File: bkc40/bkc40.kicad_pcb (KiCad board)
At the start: 2 copper layers, 266.7 x 76.2 mm, 107 parts, among them J1 Conn_01x02, SW1 SW_Push, SW10 SW_Push, SW11 SW_Push, SW12 SW_Push, SW13 SW_Push, SW14 SW_Push, SW15 SW_Push, SW16 SW_Push, SW17 SW_Push, SW18 SW_Push, SW19 SW_Push, SW2 SW_Push, SW20 SW_Push, SW21 SW_Push, SW22 SW_Push, SW23 SW_Push, SW24 SW_Push, SW25 SW_Push, SW26 SW_Push, SW27 SW_Push, SW28 SW_Push, SW29 SW_Push, SW3 SW_Push, SW30 SW_Push, SW31 SW_Push, SW32 SW_Push, SW33 SW_Push, SW34 SW_Push, SW35 SW_Push, SW36 SW_Push, SW37 SW_Push, SW38 SW_Push, SW39 SW_Push, SW4 SW_Push, SW40 SW_Push, SW41 SW_Push, SW42 SW_Push, SW43 SW_Push, SW44 SW_Push, SW45 SW_Push, SW46 SW_Push, SW47 SW_Push, SW48 SW_Push, SW49 SW_Push, SW5 SW_Push, SW50 SW_Push, SW51 SW_Push, SW52 SW_Push, SW53 SW_Push, SW54 SW_Push, SW55 SW_Push, SW56 Rotary_Encoder_Switch, SW57 SW_Push, SW6 SW_Push, SW7 SW_Push, SW8 SW_Push, SW9 SW_Push, U1 ATmega32U4-AU, Y1 Crystal_GND24_Small

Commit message: v02
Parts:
- removed the G*** at (134.0, 115.1)
- removed U1: ATmega32U4-AU, Package_QFP:TQFP-44_10x10mm_P0.8mm
- added G***: LOGO, silk:turtle_pan_800_bmask, B.Cu at (287.8, 145.4)
- added U2: ATmega32U4-MU, Package_DFN_QFN:QFN-44-1EP_7x7mm_P0.5mm_EP5.2x5.2mm, B.Cu at (143.4, 110.8)
- moved J1 243.5 mm to (118.2, 102.9), turned to 0 degrees
- moved C7 212.0 mm to (151.3, 100.2)
- moved C8 212.0 mm to (145.0, 100.3)
- moved Y1 212.0 mm to (148.2, 100.2)
- moved C1 211.9 mm to (149.3, 112.0)
- moved C2 211.5 mm to (137.2, 111.7)
- moved R4 210.2 mm to (144.2, 116.9), turned to 45 degrees
- moved C5 209.8 mm to (145.1, 104.9)
- moved C9 206.0 mm to (141.5, 103.3), turned to 45 degrees
- moved R1 205.3 mm to (146.1, 103.9), turned to 135 degrees
- moved C6 204.6 mm to (142.6, 104.2), turned to 45 degrees
- moved C4 204.0 mm to (138.4, 107.3)
- moved C3 201.8 mm to (140.9, 116.7), turned to 180 degrees
- moved D21 18.0 mm to (354.7, 120.3)
- moved C10 13.3 mm to (146.6, 80.8)
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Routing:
- net ENC_B: track 69.3 -> 355.2 mm, vias 1 -> 0
- net ENC_A: track 61.0 -> 346.5 mm, vias 1 -> 0
- net +5V: track 308.8 -> 67.9 mm, vias 4 -> 6
- net COL00: track 328.0 -> 91.4 mm, vias 0 -> 1
- net COL01: track 296.4 -> 72.4 mm
- net COL12: track 80.6 -> 297.0 mm
- net D-: track 226.1 -> 13.4 mm
- net D+: track 225.2 -> 13.7 mm
- net COL11: track 102.2 -> 287.9 mm, vias 0 -> 1
- net COL02: track 275.5 -> 93.5 mm
- net COL10: track 105.6 -> 249.1 mm, vias 0 -> 1
- net COL03: track 252.5 -> 115.2 mm
- net COL04: track 232.9 -> 112.1 mm
- net COL09: track 124.9 -> 228.8 mm, vias 0 -> 1
- net COL08: track 123.4 -> 187.7 mm, vias 0 -> 1
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
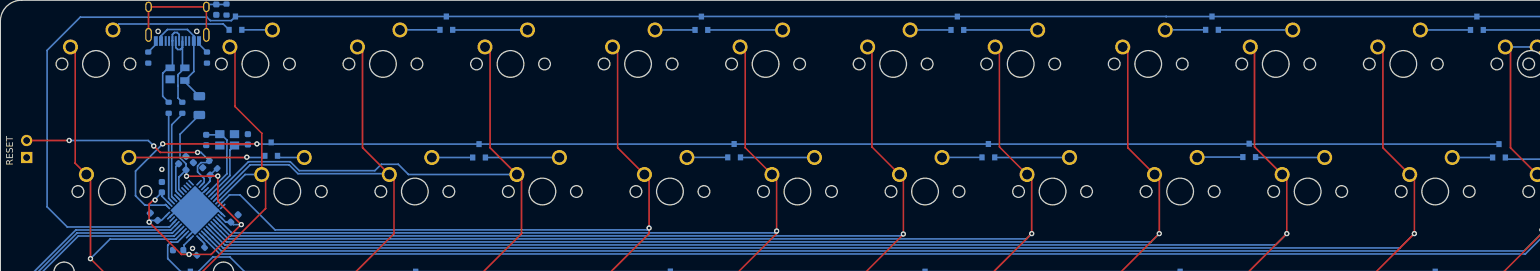
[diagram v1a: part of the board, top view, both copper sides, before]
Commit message: update cc pins
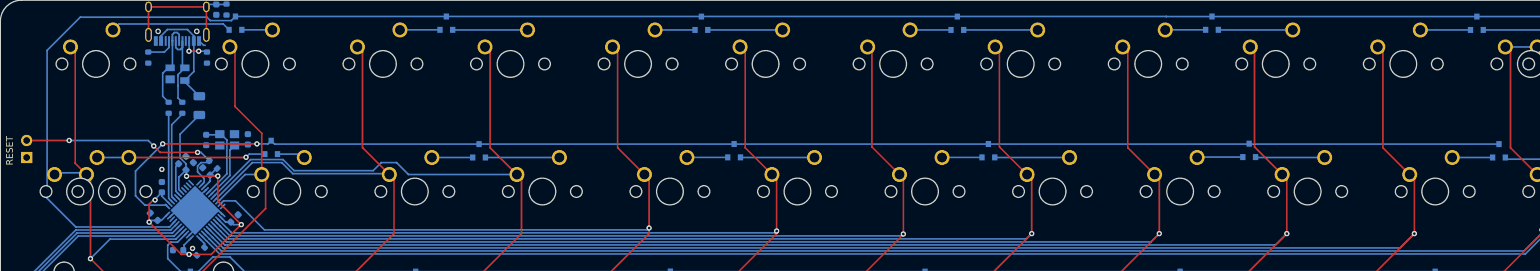
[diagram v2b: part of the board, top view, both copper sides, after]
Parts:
- added SW58: SW_Push, MX_Only:MXOnly-1.25U-NoLED, F.Cu at (126.2, 108.0)
- moved D8 0.25 mm to (154.8, 101.4)
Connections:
- USB1 pad 1: Net-(R5-Pad2) -> GND
- USB1 pad 10: Net-(USB1-Pad10) -> Net-(R6-Pad2)
- USB1 pad 12: Net-(R6-Pad2) -> GND
- USB1 pad 4: Net-(USB1-Pad4) -> Net-(R5-Pad2)
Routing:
- net COL00: track 91.4 -> 96.4 mm
- net Net-(D8-Pad2): track 20.3 -> 25.3 mm
- net Net-(R5-Pad2): track 2.12 -> 4.35 mm
- net GND: track 20.1 -> 22.2 mm
- net Net-(R6-Pad2): track 2.14 -> 4.27 mm, vias 0 -> 2
- net ROW00: track 283.2 -> 282.4 mm
- net COL04: track 112.1 -> 111.4 mm

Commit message: PCB update
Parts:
- moved J1 7.39 mm to (117.6, 110.2)
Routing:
- net Net-(J1-Pad2): track 34.2 -> 39.1 mm
- net ROW00: track 282.4 -> 284.7 mm
- net COL12: track 297.0 -> 297.5 mm
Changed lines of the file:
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@@
     (thickness 1.6)
     (drawings 11)
-    (tracks 572)
+    (tracks 573)
     (zones 0)
     (modules 108)
@@
   )
   (module Connector_PinHeader_2.54mm:PinHeader_1x02_P2.54mm_Vertical (layer B.Cu)
-    (at 118.237 102.87)
+    (at 117.602 110.236)
     (descr "Through hole straight pin header, 1x02, 2.54mm pitch, single row")
     (tags "Through hole pin header THT 1x02 2.54mm single row")
@@
     (effects (font (size 1 1) (thickness 0.15)) (justify mirror))
   )
-  (gr_text RESET (at 115.697 101.853999 90) (layer F.SilkS)
+  (gr_text RESET (at 115.316 109.092999 90) (layer F.SilkS)
     (effects (font (size 1 1) (thickness 0.15)))
   )
-  (gr_text RESET (at 115.697 101.853999 90) (layer B.SilkS)
+  (gr_text RESET (at 115.316 109.092999 90) (layer B.SilkS)
     (effects (font (size 1 1) (thickness 0.15)) (justify mirror))
   )
@@
   (segment (start 356.967 81.82) (end 357.632 81.155) (width 0.25) (layer B.Cu) (net 1))
   (segment (start 334.838 81.82) (end 356.967 81.82) (width 0.25) (layer B.Cu) (net 1))
-  (segment (start 140.315924 112.497796) (end 140.315924 112.427101) (width 0.25) (layer B.Cu) (net 1))
-  (segment (start 121.285 86.868) (end 121.285 108.966) (width 0.25) (layer B.Cu) (net 1))
-  (segment (start 126.238 81.915) (end 121.285 86.868) (width 0.25) (layer B.Cu) (net 1))
+  (segment (start 119.634 88.519) (end 119.634 108.839) (width 0.25) (layer B.Cu) (net 1))
+  (segment (start 124.042001 113.247001) (end 139.566719 113.247001) (width 0.25) (layer B.Cu) (net 1))
+  (segment (start 126.238 81.915) (end 119.634 88.519) (width 0.25) (layer B.Cu) (net 1))
+  (segment (start 119.634 108.839) (end 124.042001 113.247001) (width 0.25) (layer B.Cu) (net 1))
   (segment (start 145.161 81.915) (end 126.238 81.915) (width 0.25) (layer B.Cu) (net 1))
-  (segment (start 125.566001 113.247001) (end 139.566719 113.247001) (width 0.25) (layer B.Cu) (net 1))
-  (segment (start 121.285 108.966) (end 125.566001 113.247001) (width 0.25) (layer B.Cu) (net 1))
+  (segment (start 145.669 82.423) (end 145.161 81.915) (width 0.25) (layer B.Cu) (net 1))
   (segment (start 148.799 82.423) (end 145.669 82.423) (width 0.25) (layer B.Cu) (net 1))
+  (segment (start 140.315924 112.497796) (end 140.315924 112.427101) (width 0.25) (layer B.Cu) (net 1))
   (segment (start 139.566719 113.247001) (end 140.315924 112.497796) (width 0.25) (layer B.Cu) (net 1))
-  (segment (start 145.669 82.423) (end 145.161 81.915) (width 0.25) (layer B.Cu) (net 1))
   (segment (start 149.418 81.804) (end 148.799 82.423) (width 0.25) (layer B.Cu) (net 1))
   (segment (start 147.595 82.931) (end 148.468 83.804) (width 0.25) (layer B.Cu) (net 2))
@@
   (segment (start 365.29875 95.9) (end 365.28375 95.885) (width 0.25) (layer B.Cu) (net 54))
   (segment (start 368.987 95.9) (end 365.29875 95.9) (width 0.25) (layer B.Cu) (net 54))
-  (via (at 366.268 113.665) (size 0.8) (drill 0.4) (layers F.Cu B.Cu) (net 54))
-  (segment (start 366.268 113.792) (end 366.268 113.665) (width 0.25) (layer F.Cu) (net 54))
   (segment (start 366.268 96.647) (end 366.268 113.792) (width 0.25) (layer F.Cu) (net 54))
   (segment (start 366.268 113.792) (end 366.268 118.71325) (width 0.25) (layer F.Cu) (net 54))
-  (segment (start 145.096334 115.316) (end 144.328755 114.548421) (width 0.25) (layer B.Cu) (net 54))
-  (segment (start 147.059324 117.27899) (end 145.096334 115.316) (width 0.25) (layer B.Cu) (net 54))
-  (segment (start 342.08001 117.27899) (end 147.059324 117.27899) (width 0.25) (layer B.Cu) (net 54))
-  (segment (start 345.694 113.665) (end 342.08001 117.27899) (width 0.25) (layer B.Cu) (net 54))
-  (segment (start 366.268 113.665) (end 345.694 113.665) (width 0.25) (layer B.Cu) (net 54))
+  (via (at 366.268 113.283996) (size 0.8) (drill 0.4) (layers F.Cu B.Cu) (net 54))
+  (segment (start 147.059324 117.27899) (end 342.08001 117.27899) (width 0.25) (layer B.Cu) (net 54))
+  (segment (start 366.268 113.792) (end 366.268 113.283996) (width 0.25) (layer F.Cu) (net 54))
+  (segment (start 144.328755 114.548421) (end 147.059324 117.27899) (width 0.25) (layer B.Cu) (net 54))
+  (segment (start 342.08001 117.27899) (end 346.075004 113.283996) (width 0.25) (layer B.Cu) (net 54))
+  (segment (start 346.075004 113.283996) (end 366.268 113.283996) (width 0.25) (layer B.Cu) (net 54))
   (segment (start 131.41325 123.952) (end 131.92125 124.46) (width 0.25) (layer B.Cu) (net 55))
   (segment (start 122.90425 123.952) (end 131.41325 123.952) (width 0.25) (layer B.Cu) (net 55))
@@
   (segment (start 143.383 113.602666) (end 143.383 110.774239) (width 0.25) (layer B.Cu) (net 66))
   (segment (start 142.437245 114.548421) (end 143.383 113.602666) (width 0.25) (layer B.Cu) (net 66))
+  (segment (start 137.528 85.471) (end 137.528 85.992) (width 0.25) (layer B.Cu) (net 66))
+  (segment (start 143.978 85.471) (end 143.978 85.939) (width 0.25) (layer B.Cu) (net 66))
+  (segment (start 143.978 85.471) (end 144.018 85.471) (width 0.25) (layer B.Cu) (net 66))
+  (segment (start 144.018 85.471) (end 144.653 86.106) (width 0.25) (layer B.Cu) (net 66))
+  (segment (start 144.653 86.106) (end 144.907 86.106) (width 0.25) (layer B.Cu) (net 66))
   (segment (start 138.353705 112.268) (end 139.255264 111.366441) (width 0.25) (layer B.Cu) (net 67))
   (segment (start 147.959188 112.522) (end 147.157182 111.719994) (width 0.25) (layer B.Cu) (net 67))
@@
   (segment (start 145.796 103.632) (end 144.272 103.632) (width 0.25) (layer B.Cu) (net 74))
   (via (at 124.587 100.33) (size 0.8) (drill 0.4) (layers F.Cu B.Cu) (net 74))
-  (segment (start 118.237 100.33) (end 124.587 100.33) (width 0.25) (layer F.Cu) (net 74))
   (via (at 137.218847 101.150847) (size 0.8) (drill 0.4) (layers F.Cu B.Cu) (net 74))
   (segment (start 136.398 100.33) (end 137.218847 101.150847) (width 0.25) (layer B.Cu) (net 74))
@@
   (segment (start 144.272 102.108) (end 145.518274 103.354274) (width 0.25) (layer B.Cu) (net 74))
   (segment (start 143.764 102.108) (end 144.272 102.108) (width 0.25) (layer B.Cu) (net 74))
+  (segment (start 122.936 100.33) (end 124.587 100.33) (width 0.25) (layer F.Cu) (net 74))
+  (segment (start 117.602 105.664) (end 122.936 100.33) (width 0.25) (layer F.Cu) (net 74))
+  (segment (start 117.602 107.696) (end 117.602 105.664) (width 0.25) (layer F.Cu) (net 74))
   (segment (start 139.446 108.958559) (end 139.962371 109.47493) (width 0.25) (layer B.Cu) (net 75))
   (segment (start 139.446 96.265) (end 139.446 108.958559) (width 0.25) (layer B.Cu) (net 75))
@@
   (segment (start 144.803726 115.730499) (end 143.975202 114.901975) (width 0.25) (layer B.Cu) (net 77))
   (segment (start 144.803726 116.308274) (end 144.803726 115.730499) (width 0.25) (layer B.Cu) (net 77))
-  (segment (start 137.528 85.471) (end 137.528 85.992) (width 0.25) (layer B.Cu) (net 66))
-  (segment (start 143.978 85.471) (end 143.978 85.939) (width 0.25) (layer B.Cu) (net 66))
-  (segment (start 143.978 85.471) (end 144.018 85.471) (width 0.25) (layer B.Cu) (net 66))
-  (segment (start 144.018 85.471) (end 144.653 86.106) (width 0.25) (layer B.Cu) (net 66))
-  (segment (start 144.653 86.106) (end 144.907 86.106) (width 0.25) (layer B.Cu) (net 66))
   (segment (start 138.812002 87.122) (end 136.398 87.122) (width 0.25) (layer B.Cu) (net 78))
   (segment (start 139.503 86.431002) (end 138.812002 87.122) (width 0.25) (layer B.Cu) (net 78))
